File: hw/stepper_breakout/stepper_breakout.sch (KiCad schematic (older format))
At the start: 19 parts, among them P1 X_HOME, P10 A, P11 Y, P12 POWER_IN, P13 B, P14 X, P15 CONN_02X25, P2 Y_HOME, P3 Z_HOME, P4 A_HOME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

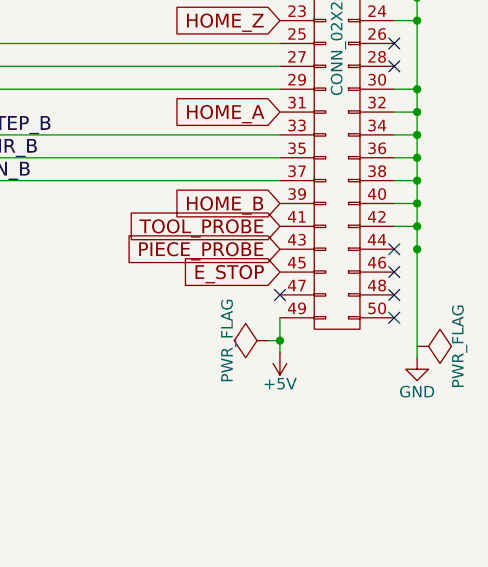
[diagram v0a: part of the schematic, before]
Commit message: Adjust track width in stepper breakout
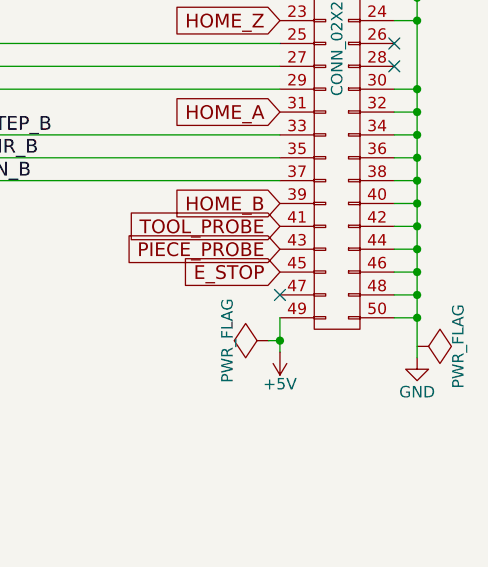
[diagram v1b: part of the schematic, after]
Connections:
- net GND: now also P15.44 (P44), P15.46 (P46), P15.48 (P48), P15.50 (P50)
- no-connect marks 9 -> 5
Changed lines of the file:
@@
 NoConn ~ 8950 3350
 Connection ~ 9050 4150
-NoConn ~ 8950 4450
-NoConn ~ 8950 4350
-NoConn ~ 8950 4250
-NoConn ~ 8950 4150
+Wire Wire Line
+	8950 4150 9050 4150
+Wire Wire Line
+	8950 4250 9050 4250
+Connection ~ 9050 4250
+Wire Wire Line
+	8950 4350 9050 4350
+Connection ~ 9050 4350
+Wire Wire Line
+	8950 4450 9050 4450
+Connection ~ 9050 4450
 $EndSCHEMATC
